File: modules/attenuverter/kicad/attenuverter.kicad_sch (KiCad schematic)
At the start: 23 parts, among them J1 IN 1, J2 OUT 1, J3 IN 2, J4 OUT 2, J5 POWER, U1 TL072

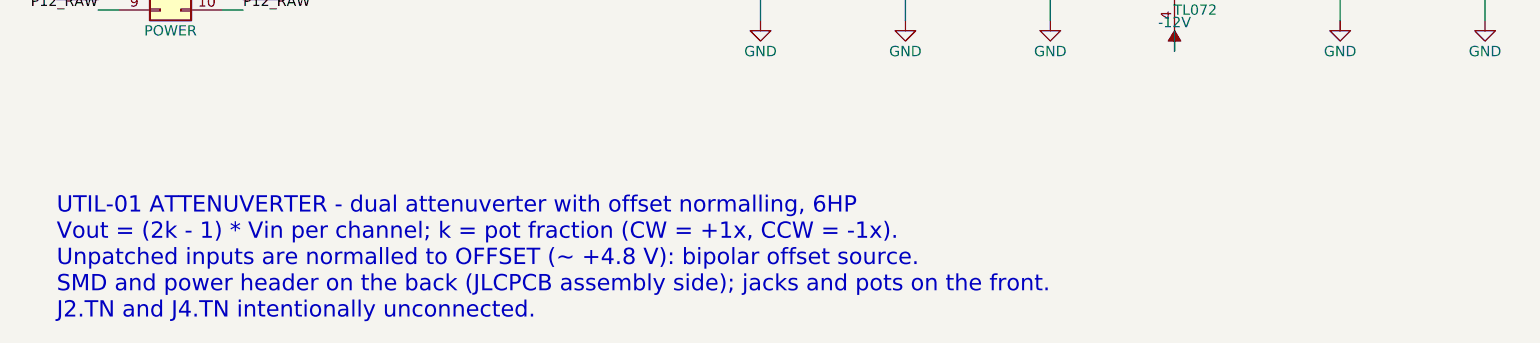
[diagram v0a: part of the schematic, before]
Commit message: M4: derive the attenuverter precision error budget; open the parts decision
docs/modules/attenuverter/ERROR-BUDGET.md derives, from the TL072C, UNI-ROYAL
resistor, Alpha RD901F, OPA2197 and REF5050 datasheets fetched today, how far
the output can stray from (2k-1)*Vin and from a stable offset, in volts and in
cents at 1 V/octave. Beyond the known 41.8 mV shared-reference shift it finds a
27 mV worst-case offset, a 2.3 % inversion error, an output swing and input
common-mode range the TL072C does not guarantee at +/-10 V, no feedback
compensation, and a 50 k input impedance that loads a 1 k source 2 %. The
Mutable Instruments Shades v4.0 BOM and Befaco Dual Attenuverter v2 guide are
the reference designs consulted.

docs/decisions/2026-09-11-attenuverter-precision-parts.md asks the user to
choose between a parts swap in the same topology (OPA2197, 0.1 % thin film,
REF5050A, 10 pF) and the same plus a unity-gain input buffer per channel, with
LCSC prices and stock at quantity 10; B is recommended. Nothing is implemented
until it is answered.

Also: cabal.project.freeze pins the Haskell dependencies (M3); the routing
report says matched-group lengths count 1.6 mm per via; the attenuverter's
comments and schematic note give the simulated 4.67 V reference; AGENTS.md
lists modules/_tests/. Regenerated, ERC/DRC clean, 65/65 tests, 6 decks pass.

Co-Authored-By: Claude Fable 5.1 <noreply@anthropic.com>
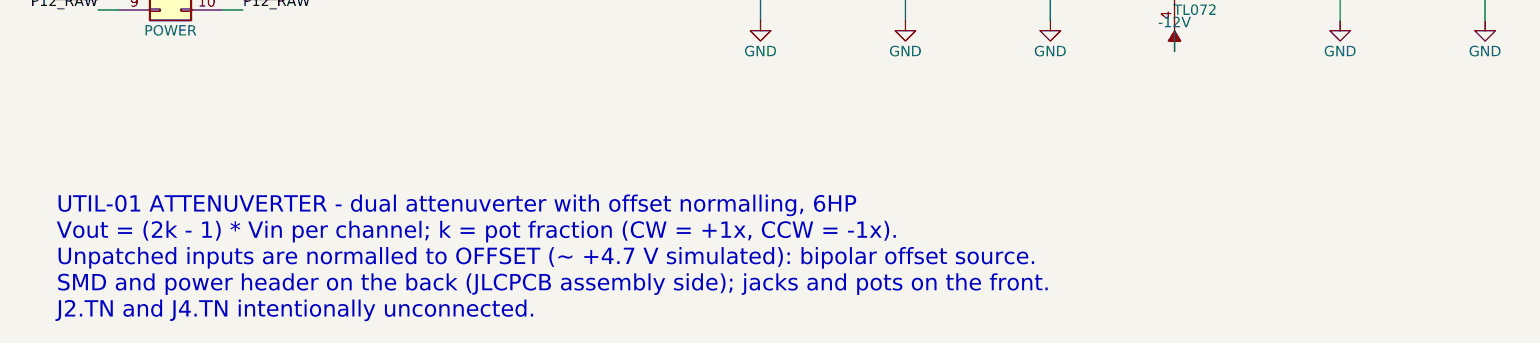
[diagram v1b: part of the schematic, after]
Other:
- note added: "UTIL-01 ATTENUVERTER - dual attenuverter with offset normalling, 6HP Vout = (2k - 1) * Vin per channel; k = pot fraction (CW = +1x, CCW = -1x). Unpatched inputs are normalled to OFFSET (~ +4.7 V simulated): bipolar offset source. SMD and power header on the back (JLCPCB assembly side); jacks and pots on the front. J2.TN and J4.TN intentionally unconnected."
- note removed: "UTIL-01 ATTENUVERTER - dual attenuverter with offset normalling, 6HP Vout = (2k - 1) * Vin per channel; k = pot fraction (CW = +1x, CCW = -1x). Unpatched inputs are normalled to OFFSET (~ +4.8 V): bipolar offset source. SMD and power header on the back (JLCPCB assembly side); jacks and pots on the front. J2.TN and J4.TN intentionally unconnected."
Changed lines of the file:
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@@
 		)
 	)
-	(text "UTIL-01 ATTENUVERTER - dual attenuverter with offset normalling, 6HP\nVout = (2k - 1) * Vin per channel; k = pot fraction (CW = +1x, CCW = -1x).\nUnpatched inputs are normalled to OFFSET (~ +4.8 V): bipolar offset source.\nSMD and power header on the back (JLCPCB assembly side); jacks and pots on the front.\nJ2.TN and J4.TN intentionally unconnected."
+	(text "UTIL-01 ATTENUVERTER - dual attenuverter with offset normalling, 6HP\nVout = (2k - 1) * Vin per channel; k = pot fraction (CW = +1x, CCW = -1x).\nUnpatched inputs are normalled to OFFSET (~ +4.7 V simulated): bipolar offset source.\nSMD and power header on the back (JLCPCB assembly side); jacks and pots on the front.\nJ2.TN and J4.TN intentionally unconnected."
 		(exclude_from_sim no)
 		(at 25.4 190.5 0)

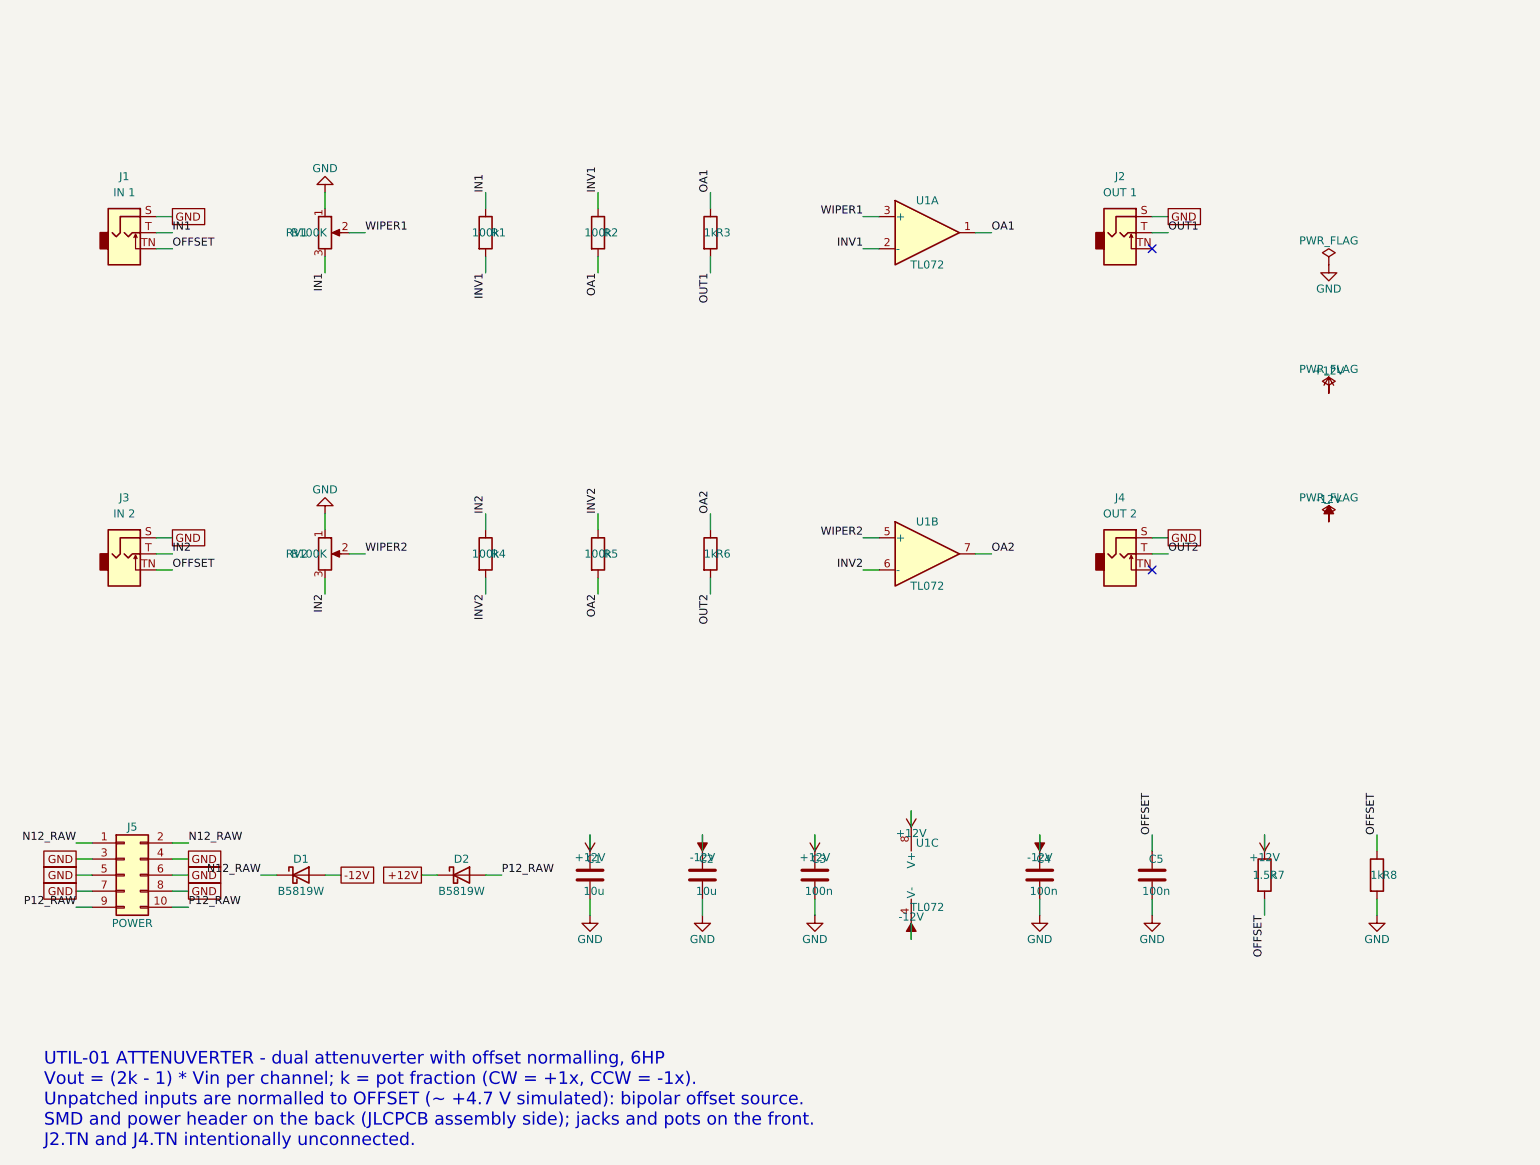
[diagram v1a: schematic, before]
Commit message: Attenuverter option B: precision circuit, models, eight decks, 100 mm boards
The attenuverter becomes the option B design the user chose: one OPA2197
per channel as unity-gain input buffer plus attenuverter stage, 10k 0.1%
thin-film gain resistors with 10 pF C0G compensation, a 1M input and a
REF5050 offset reference. OPA2197 and REF5050 models are built from the
datasheet maxima with input capacitance, a second pole and TEMPER terms.
Emit.Spice learns Reference_Voltage symbols and places a 0 V probe in every
op-amp output so a deck can measure loop gain by voltage injection on the
generated netlist. Eight decks assert every limit in the error budget and
pass: the stage has 72 degrees of phase margin with the capacitor and 27
without; the gain resistors are 10k rather than the assumed 100k because
the input capacitance shelved the full-clockwise response 4.6 % at 20 kHz
with 100k. eurorackPcbHeight drops to 100 mm for every module; the
attenuverter's SMD moves into the pad-free strips between its controls.
65 tests, both pipelines and sim.sh pass; the decision file is retired
into SPEC.md.

Co-Authored-By: Claude Fable 5.1 <noreply@anthropic.com>
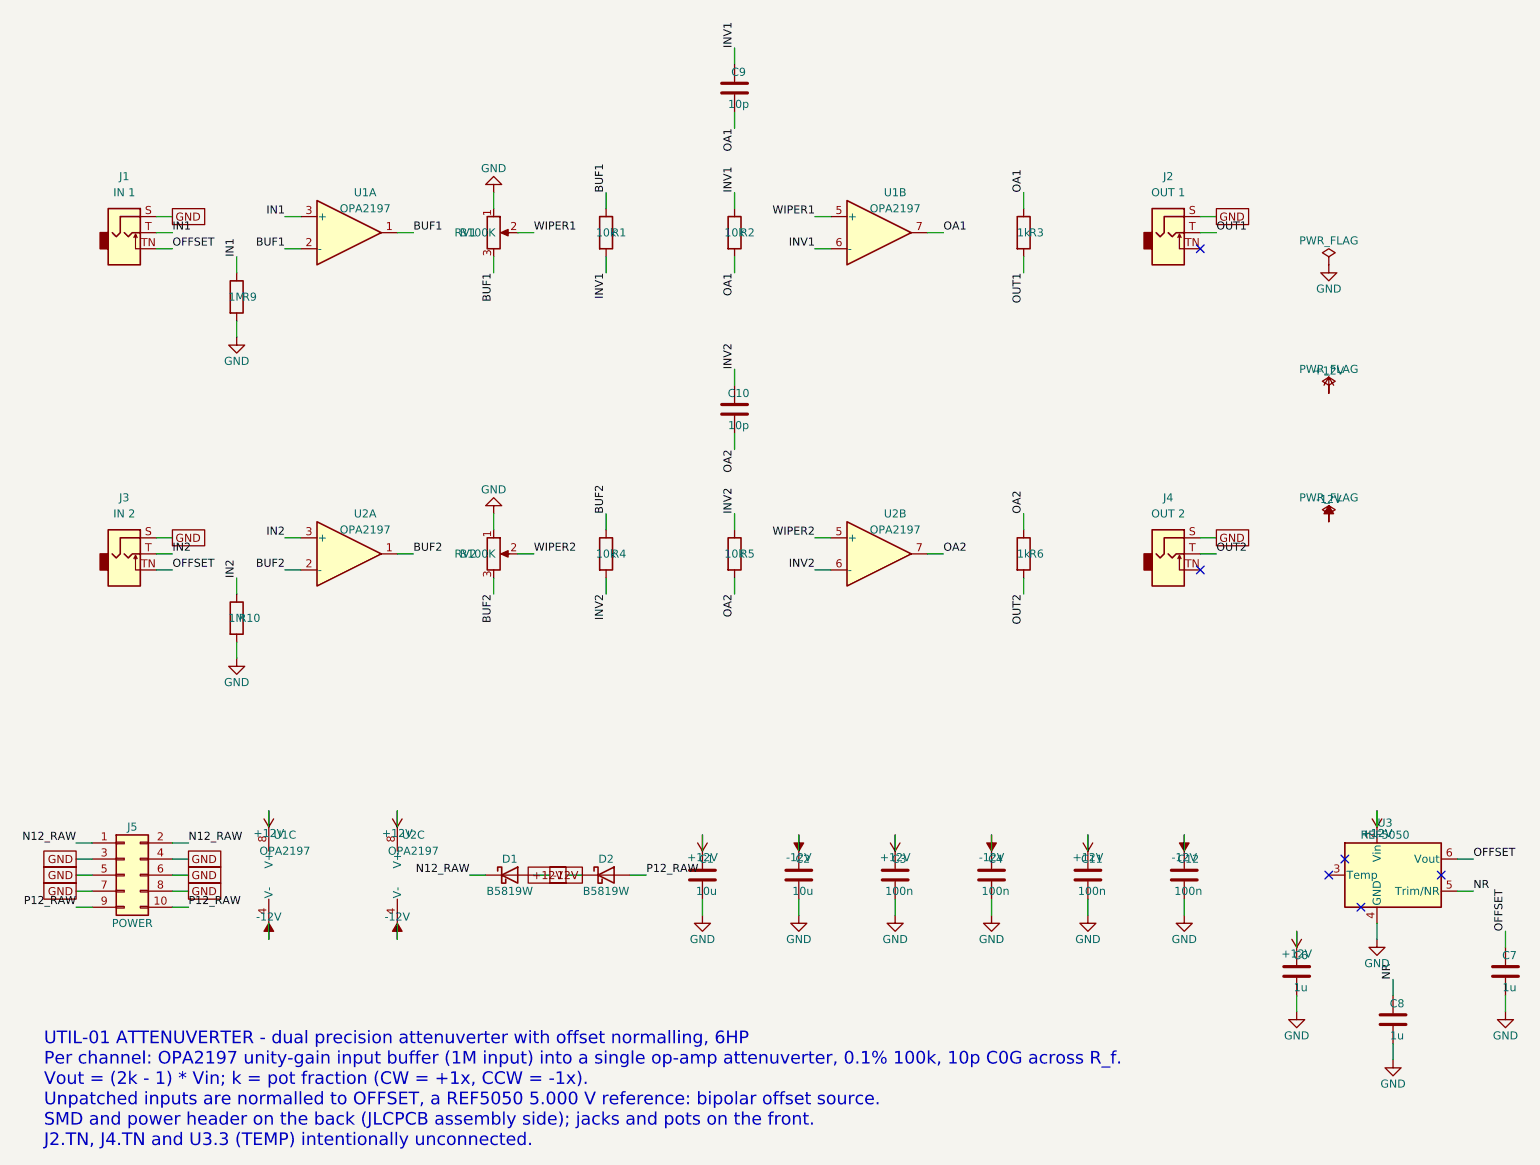
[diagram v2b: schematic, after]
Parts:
- removed C5: 100n, Capacitor_SMD:C_0805_2012Metric, symbol Device:C
- removed R7: 1.5k, Resistor_SMD:R_0805_2012Metric, symbol Device:R
- removed R8: 1k, Resistor_SMD:R_0805_2012Metric, symbol Device:R
- added C10, C9: 10p, Capacitor_SMD:C_0805_2012Metric, symbol Device:C
- added C11, C12: 100n, Capacitor_SMD:C_0805_2012Metric, symbol Device:C
- added C6, C7, C8: 1u, Capacitor_SMD:C_0805_2012Metric, symbol Device:C
- added R10, R9: 1M, Resistor_SMD:R_0805_2012Metric, symbol Device:R
- added U2: OPA2197, Package_SO:SOIC-8_3.9x4.9mm_P1.27mm, symbol Amplifier_Operational:OPA2197xD
- added U3: REF5050, Package_SO:SOIC-8_3.9x4.9mm_P1.27mm, symbol Reference_Voltage:REF5050AD
- R1, R2, R4, R5: value 100k -> 10k; LCSC Part # C17407 -> C110775
- U1: value TL072 -> OPA2197; symbol Amplifier_Operational:TL072 -> Amplifier_Operational:OPA2197xD; LCSC Part # C6961 -> C139363
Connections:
- net +12V: now also C11.1, C6.1, U2.8 (V+), U3.2 (Vin)
- net -12V: now also C12.1, U2.4 (V-)
- net GND: now also C11.2, C12.2, C6.2, C7.2, C8.2, R10.2, R9.2, U3.4 (GND)
- net IN1: now also U1.3 (+), R9.1; no longer R1.1, RV1.3
- net IN2: now also R10.1, U2.3 (+); no longer R4.1, RV2.3
- net INV1: now also U1.6 (-), C9.1; no longer U1.2 (-)
- net INV2: now also C10.1, U2.6 (-); no longer U1.6 (-)
- net OA1: now also U1.7, C9.2; no longer U1.1
- net OA2: now also C10.2, U2.7; no longer U1.7
- net OFFSET: now also C7.1, U3.6 (Vout)
- net WIPER1: now also U1.5 (+); no longer U1.3 (+)
- net WIPER2: now also U2.5 (+); no longer U1.5 (+)
- new net BUF1: R1.1, RV1.3, U1.1, U1.2 (-)
- new net BUF2: R4.1, RV2.3, U2.1, U2.2 (-)
- new net NR: C8.1, U3.5 (Trim/NR)
- no-connect marks 2 -> 6
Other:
- note added: "UTIL-01 ATTENUVERTER - dual precision attenuverter with offset normalling, 6HP Per channel: OPA2197 unity-gain input buffer (1M input) into a single op-amp attenuverter, 0.1% 100k, 10p C0G across R_f. Vout = (2k - 1) * Vin; k = pot fraction (CW = +1x, CCW = -1x). Unpatched inputs are normalled to OFFSET, a REF5050 5.000 V reference: bipolar offset source. SMD and power header on the back (JLCPCB 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"
- note removed: "UTIL-01 ATTENUVERTER - dual attenuverter with offset normalling, 6HP Vout = (2k - 1) * Vin per channel; k = pot fraction (CW = +1x, CCW = -1x). Unpatched inputs are normalled to OFFSET (~ +4.7 V simulated): bipolar offset source. SMD and power header on the back (JLCPCB assembly side); jacks and pots on the front. J2.TN and J4.TN intentionally unconnected."
- moved on the sheet: C1, C2, C3, C4, D1, D2, J2, J4, R1, R2, R3, R4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

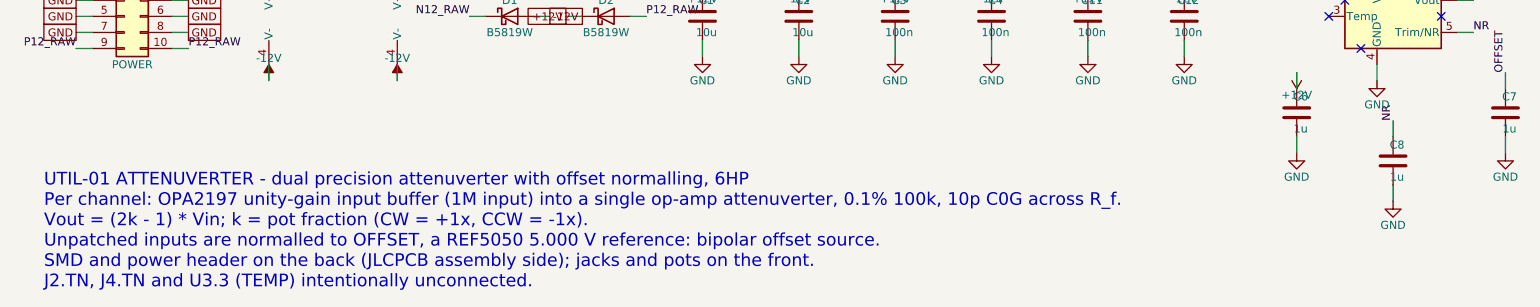
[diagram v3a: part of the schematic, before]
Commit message: Factor the buffered attenuverter channel into Block.Precision
The option B channel (OPA2197 unity-gain buffer into a single op-amp
attenuverter, 10k 0.1 % gain pair with 10 pF C0G, 1M input, 1k output,
100 nF at each supply pin) becomes Block.Precision, the block that will
reappear on every CV input of the five-board system. The block owns the
parts' identities and the nets, including the channel's pins on the rails;
Attenuverter.hs only places it in the two SMD strips. The sheet note is
corrected from 100k to 10k, which it had said since the option B decks
changed the value.

Acceptance: the regenerated board is identical to the previous checkpoint
up to line order (zero differing lines sorted); the schematic differs only
in that note. Module and panel pass ERC and DRC with schematic parity, the
mult pipeline passes, the eight decks pass on the block-built netlist, and
80/80 tests pass with two new block tests pinning the channel's parts,
values, LCSC numbers and every pin's net.

Co-Authored-By: Claude Fable 5.1 <noreply@anthropic.com>
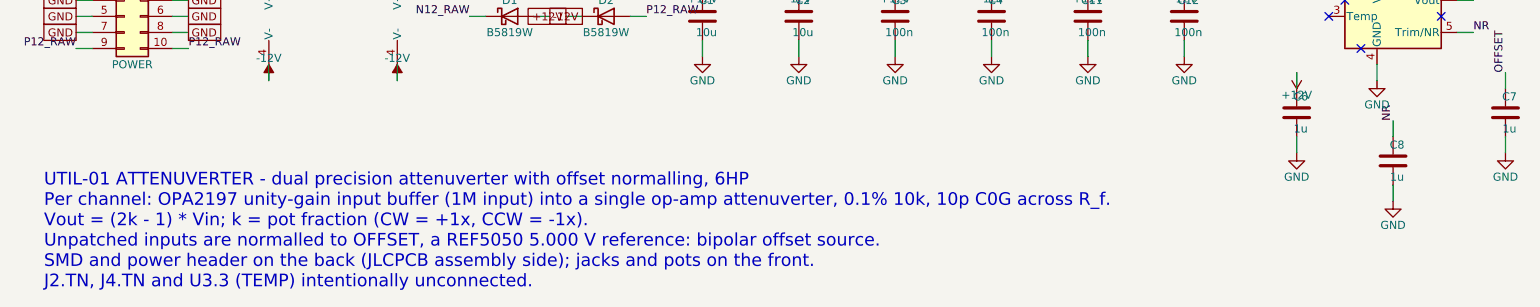
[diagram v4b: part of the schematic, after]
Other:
- note added: "UTIL-01 ATTENUVERTER - dual precision attenuverter with offset normalling, 6HP Per channel: OPA2197 unity-gain input buffer (1M input) into a single op-amp attenuverter, 0.1% 10k, 10p C0G across R_f. Vout = (2k - 1) * Vin; k = pot fraction (CW = +1x, CCW = -1x). Unpatched inputs are normalled to OFFSET, a REF5050 5.000 V reference: bipolar offset source. SMD and power header on the back (JLCPCB a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"
- note removed: "UTIL-01 ATTENUVERTER - dual precision attenuverter with offset normalling, 6HP Per channel: OPA2197 unity-gain input buffer (1M input) into a single op-amp attenuverter, 0.1% 100k, 10p C0G across R_f. Vout = (2k - 1) * Vin; k = pot fraction (CW = +1x, CCW = -1x). Unpatched inputs are normalled to OFFSET, a REF5050 5.000 V reference: bipolar offset source. SMD and power header on the back (JLCPCB 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"
